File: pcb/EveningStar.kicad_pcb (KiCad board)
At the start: 2 copper layers, 145.5 x 43.6 mm, 152 parts, among them J1 PZ254V-11-02P, J2 Connector, USB-TYPE-C-16P, J3 ESPPROG, J4 RJ45_Hanrun_HR911105A_Horizon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, Q2 AO3400A, U1 TPS5430DDAR, U10 AMS1117-5.0, U11 AMS1117-3.3, U2 SN74HC132DR, U3 ISO6721RBDR, U4 DC-005H-D020, U5 15uH, U6 AHT20-F, U8 ESP32-C6-MINI-1U-H4, U9 W5500, Y1 25MHz

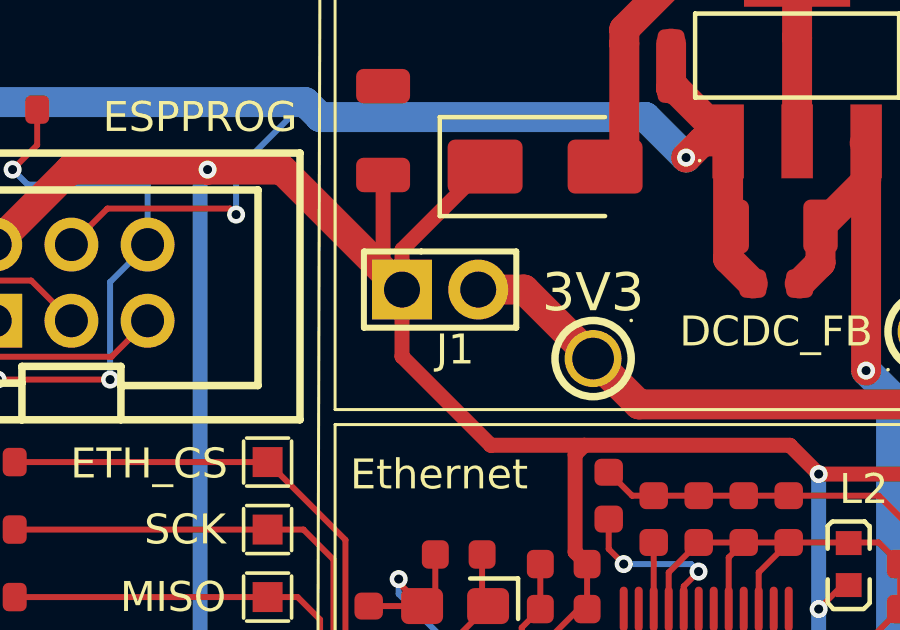
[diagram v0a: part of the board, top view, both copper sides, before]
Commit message: sch: remove 3.3v jumper
Fixes #16
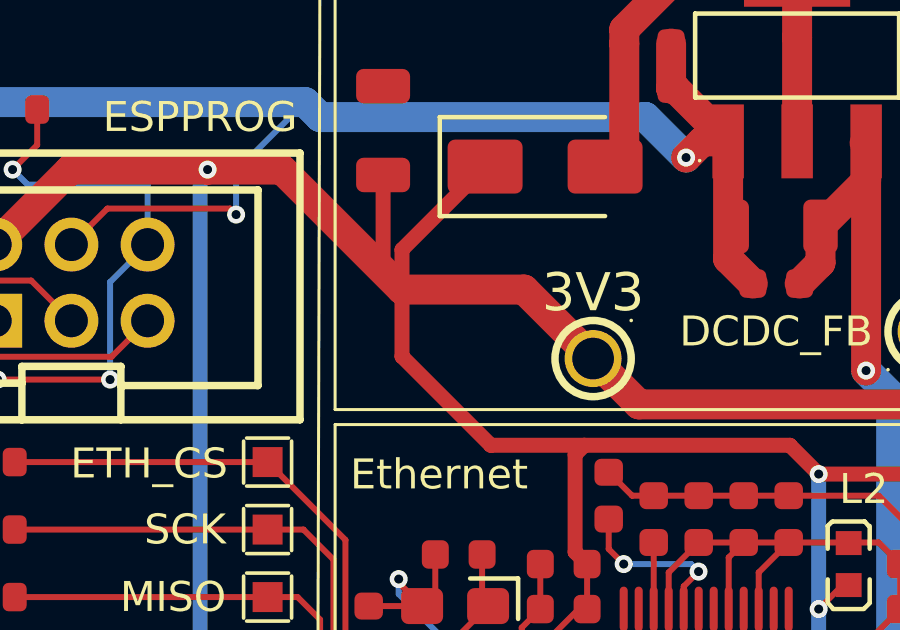
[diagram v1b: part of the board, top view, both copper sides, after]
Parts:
- removed J1: PZ254V-11-02P, EasyEDA:HDR-TH_2P-P2.54-V-M
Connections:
- C36 pad 1: Net-(J1-Pin_2) -> +3V3
- C8 pad 1: Net-(J1-Pin_2) -> +3V3
- R12 pad 1: Net-(J1-Pin_2) -> +3V3
- TP10 pad 1: Net-(J1-Pin_2) -> +3V3
- U5 pad 2: Net-(J1-Pin_2) -> +3V3
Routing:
- net +3V3: track 245.9 -> 282.6 mm
- net Net-(J1-Pin_2): track 34.6 -> 0.00 mm
- added copper zone on F.Cu, net +3V3
- removed copper zone on F.Cu, net Net-(J1-Pin_2)

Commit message: pcb: layout and route meterbus frontend
Places parts PCB traces for MeterBus frontend.
Also changes which gates on HC14 schematic are used to simplify routing.
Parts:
- removed C36, C39: 100uF, PCM_JLCPCB:C_1206
- removed C37: 100nF, PCM_JLCPCB:C_0603
- removed C38: 150pF, PCM_JLCPCB:C_0603
- removed C45: 10uF, PCM_JLCPCB:C_0805
- removed D10, D11: SMAJ28CA, PCM_JLCPCB:D_DO-214AC(SMA)
- removed D14, D8: SS210, PCM_JLCPCB:D_SMA
- removed D9: SS14, PCM_JLCPCB:D_SMA
- removed J3: ESPPROG, EasyEDA:IDC-TH_6P-P2.54-V-R2-C3-S2.54
- removed J4: RJ45_Hanrun_HR911105A_Horizontal, EasyEDA:RJ45-TH_HR911105A
- removed Q2: AO3400A, PCM_JLCPCB:Q_SOT-23
- removed R27: 33Ω, PCM_JLCPCB:R_0603
- removed R28, R29, R30: 10kΩ, PCM_JLCPCB:R_0603
- removed R48: 12kΩ, PCM_JLCPCB:R_0603
- removed R49: 200Ω, PCM_JLCPCB:R_0603
- removed R5: 100Ω, PCM_JLCPCB:R_0603
- removed R53, R54: 2Ω, PCM_JLCPCB:R_0603
- removed S2, S3: Tactile Button, 160gf, PCM_JLCPCB:SW_TS-1088-AR02016
- removed TP1, TP12, TP13, TP2, TP3, TP5, TP6, TP7, TP8, TP9: RH-5001, EasyEDA:TEST-TH_BD2.54-P1.4_BLACK
- removed U10: AMS1117-5.0, EasyEDA:SOT-223_L6.5-W3.5-P2.30-LS7.0-BR
- removed U2: SN74HC132DR, EasyEDA:SOIC-14_L8.7-W3.9-P1.27-LS6.0-BL
- removed U4: DC-005H-D020, EasyEDA:DC-IN-TH_G-SWITCH_DC-005H-D020
- added C11: 20pF, PCM_JLCPCB:C_0603, F.Cu at (809.0, -32.6)
- added C12: 20pF, PCM_JLCPCB:C_0603, F.Cu at (809.0, -30.4)
- added C14: 100nF, PCM_JLCPCB:C_0805, F.Cu at (908.2, -95.6)
- added D1: USBLC6-2P6, EasyEDA:SOT-666-6_L1.6-W1.2-P0.50-LS1.6-BR, F.Cu at (1062.4, -97.3)
- added D15: SS210, PCM_JLCPCB:D_SMA, F.Cu at (926.0, -91.5)
- added D3: SMBJ17CA, EasyEDA:SMB_L4.3-W3.6-LS5.4-BI, F.Cu at (584.5, 24.0)
- added F1: 1A, EasyEDA:FUSE-SMD_L6.1-W2.6, F.Cu at (926.5, -101.1)
- added P1: WJ15EDGRC-3.81-2P, EasyEDA:CONN-TH_2P-P3.81_WJ15EDGRC-3.81-2P, F.Cu at (916.5, -111.6)
- added Q1: 2N7002, PCM_JLCPCB:Q_SOT-23, F.Cu at (605.0, 31.5)
- added R37: 33Ω, PCM_JLCPCB:R_0603, F.Cu at (865.6, 17.9)
- added R50: 33Ω, PCM_JLCPCB:R_0603, F.Cu at (867.9, 17.9)
- added R55: 33Ω, PCM_JLCPCB:R_0603, F.Cu at (812.5, -58.0)
- added R57: 10kΩ, PCM_JLCPCB:R_0603, F.Cu at (812.5, -55.8)
- added R58: 10kΩ, PCM_JLCPCB:R_0603, F.Cu at (812.5, -53.5)
- added R59: 10kΩ, PCM_JLCPCB:R_0603, F.Cu at (812.5, -51.3)
- added R60: 10kΩ, PCM_JLCPCB:R_0603, F.Cu at (970.8, -31.5)
- added R61: 10kΩ, PCM_JLCPCB:R_0603, F.Cu at (970.8, -29.2)
- added R62: 33Ω, PCM_JLCPCB:R_0603, F.Cu at (812.5, -49.0)
- added R63: 33Ω, PCM_JLCPCB:R_0603, F.Cu at (816.2, -58.0)
- added R64: 33Ω, PCM_JLCPCB:R_0603, F.Cu at (816.2, -55.8)
- added R65: 33Ω, PCM_JLCPCB:R_0603, F.Cu at (816.2, -53.5)
- added R66: 10kΩ, PCM_JLCPCB:R_0603, F.Cu at (970.8, -27.0)
- added RJ2: 5201-6P6C, EasyEDA:RJ45-TH_RRCH-5201-6P6C, F.Cu at (593.8, 24.2)
- added TP24: READ_ISO, TestPoint:TestPoint_Pad_D1.0mm, F.Cu at (617.5, 21.0)
- added TP25: GND_ISO, TestPoint:TestPoint_Plated_Hole_D2.0mm, F.Cu at (605.0, 27.5)
- added TP26: MB_PWR_ISO, TestPoint:TestPoint_Plated_Hole_D2.0mm, F.Cu at (584.5, 31.5)
- added TP27: WRITE_ISO, TestPoint:TestPoint_Pad_D1.0mm, F.Cu at (617.5, 23.5)
- added TP28: READ, TestPoint:TestPoint_Pad_D1.0mm, F.Cu at (634.5, 21.0)
- added TP29: WRITE, TestPoint:TestPoint_Pad_D1.0mm, F.Cu at (640.5, 21.2)
- added TP30: MISO, TestPoint:TestPoint_Pad_D1.0mm, F.Cu at (967.5, -34.9)
- added TP31: GND, TestPoint:TestPoint_Plated_Hole_D2.0mm, F.Cu at (975.0, -32.5)
- added TP32: GND, TestPoint:TestPoint_Plated_Hole_D2.0mm, F.Cu at (813.2, -31.4)
- added TP33: FLASH_SCK, TestPoint:TestPoint_Pad_D1.0mm, F.Cu at (967.5, -31.8)
- added TP34: MOSI, TestPoint:TestPoint_Pad_D1.0mm, F.Cu at (815.7, -43.3)
- added TP35: +3V3A, TestPoint:TestPoint_Pad_D1.0mm, F.Cu at (857.7, 15.2)
- added TP36: VIN_PROTECTED, TestPoint:TestPoint_Plated_Hole_D2.0mm, F.Cu at (917.6, -92.9)
- added U7: ESP32-C6-WROOM-1-N8, EasyEDA:WIRELM-SMD_ESP32-C6-WROOM-1, F.Cu at (797.0, -42.8)
- added USB1: GT-USB-7055BB, EasyEDA:USB-C-TH_GT-USB-7055BB, F.Cu at (1062.2, -102.0)
- added X1: 32.768kHz, PCM_JLCPCB:FC-135R_L3.2-W1.5, F.Cu at (793.8, -30.9)
- C10: value 10nF -> 47uF; footprint PCM_JLCPCB:C_0603 -> PCM_JLCPCB:C_1206
- C15: value 10uF -> 47uF; footprint PCM_JLCPCB:C_0603 -> PCM_JLCPCB:C_1206
- C2: value 1uF -> 100nF
- C40: footprint PCM_JLCPCB:C_1206 -> PCM_JLCPCB:C_0603
- C42: value 100nF -> 4.7uF; footprint PCM_JLCPCB:C_0603 -> PCM_JLCPCB:C_1206
- C43: value 10uF -> 4.7uF; footprint PCM_JLCPCB:C_0603 -> PCM_JLCPCB:C_1206
- C8: value 1nF -> 22uF
- C9: value 100nF -> 47uF; footprint PCM_JLCPCB:C_0603 -> PCM_JLCPCB:C_1206
- D2: value PSM712-LF-T7 -> SMBJ40CA_C151262; footprint PCM_JLCPCB:SOT-23-3_L3.0-W1.7-P0.95-LS2.9-BR -> EasyEDA:SMB_L4.6-W3.6-LS5.3-BI
- D7: value SMAJ28CA -> PSM712-LF-T7; footprint PCM_JLCPCB:D_DO-214AC(SMA) -> PCM_JLCPCB:SOT-23-3_L3.0-W1.7-P0.95-LS2.9-BR
- J2: value Connector, USB-TYPE-C-16P -> DEBUG; footprint PCM_JLCPCB:TYPE-C-SMD_HX-TYPE-C-16PIN -> Connector_PinHeader_2.54mm:PinHeader_2x03_P2.54mm_Vertical
- R1: value 100Ω -> 1.8kΩ
- R11: value 100Ω -> 100kΩ
- R12: value 10kΩ -> 0Ω
- R13: value 5.6kΩ -> 10kΩ
- R14: value 300Ω -> 100Ω
- R15: value 10kΩ -> 62kΩ
- R16: value 10kΩ -> 27kΩ
- R2: value 1MΩ -> 100kΩ
- R23: value 33Ω -> 10MΩ
- R24: value 33Ω -> 10kΩ
- R25: value 33Ω -> 0Ω
- R26: value 33Ω -> 62kΩ
- R3: value 100kΩ -> 1MΩ
- R4: value 2MΩ -> 2.4kΩ
- R51: value 470Ω -> 33Ω
- R52: value 75Ω -> 10kΩ
- R6: value 330Ω -> 10kΩ
- R7: value 100kΩ -> 0Ω
- R8: value 330Ω -> 33Ω
- RJ1: value 5301-6P6C -> GR01M1HXA001; footprint EasyEDA:RJ45-TH_5301-6P6C -> EasyEDA:RJ45-TH_GR01M1HXA001
- TP10: value RH-5001 -> ETH_CS; footprint EasyEDA:TEST-TH_BD2.54-P1.4_BLACK -> TestPoint:TestPoint_Pad_D1.0mm
- TP11: value RH-5001 -> ETH_RST; footprint EasyEDA:TEST-TH_BD2.54-P1.4_BLACK -> TestPoint:TestPoint_Pad_D1.0mm
- TP14: value RH-5001 -> ETH_SCK; footprint EasyEDA:TEST-TH_BD2.54-P1.4_BLACK -> TestPoint:TestPoint_Pad_D1.0mm
- TP15: value RH-5001 -> FLASH_CS; footprint EasyEDA:TEST-TH_BD2.54-P1.4_BLACK -> TestPoint:TestPoint_Pad_D1.0mm
- TP16: value RH-5001 -> MISO; footprint EasyEDA:TEST-TH_BD2.54-P1.4_BLACK -> TestPoint:TestPoint_Pad_D1.0mm
- TP17: value RH-5001 -> MOSI; footprint EasyEDA:TEST-TH_BD2.54-P1.4_BLACK -> TestPoint:TestPoint_Pad_D1.0mm
- TP18: value TestPad -> ETH_INT; footprint EasyEDA:TestPoint_Pad_1.0x1.0mm -> TestPoint:TestPoint_Pad_D1.0mm
- TP19: value TestPad -> GND; footprint EasyEDA:TestPoint_Pad_1.0x1.0mm -> TestPoint:TestPoint_Plated_Hole_D2.0mm
- TP20: value TestPad -> MISO; footprint EasyEDA:TestPoint_Pad_1.0x1.0mm -> TestPoint:TestPoint_Pad_D1.0mm
- TP21: value TestPad -> VCC_ISO; footprint EasyEDA:TestPoint_Pad_1.0x1.0mm -> TestPoint:TestPoint_Pad_D1.0mm
- TP22: value TestPad -> BUS_ISO; footprint EasyEDA:TestPoint_Pad_1.0x1.0mm -> TestPoint:TestPoint_Pad_D1.0mm
- TP23: value TestPad -> MOSI; footprint EasyEDA:TestPoint_Pad_1.0x1.0mm -> TestPoint:TestPoint_Pad_D1.0mm
- U1: value TPS5430DDAR -> 78L05G; footprint EasyEDA:ESOP-8_L4.9-W3.9-P1.27-LS6.0-TL-EP -> PCM_JLCPCB:SOT-89-3_L4.5-W2.5-P1.50-LS4.2-BR
- U11: value AMS1117-3.3 -> 15uH; footprint EasyEDA:SOT-223_L6.5-W3.5-P2.30-LS7.0-BR -> EasyEDA:IND-SMD_L7.1-W6.6
- U5: value 15uH -> 74HC14D; footprint EasyEDA:IND-SMD_L7.1-W6.6 -> PCM_JLCPCB:SOIC-14_L8.7-W3.9-P1.27-LS6.0-BL
- U6: value AHT20-F -> LMR38020SDDAR; footprint EasyEDA:SENSOR-SMD-6_AHT20 -> EasyEDA:ESOP-8_L4.9-W3.9-P1.27-LS6.0-BL-EP-1
- U8: value ESP32-C6-MINI-1U-H4 -> GD5F2GM7UEYIGR; footprint EasyEDA:WIFIM-SMD_61P-L13.2-W12.5-P0.80 -> EasyEDA:WSON-8_L8.0-W6.0-P1.27-TL-1
- U9: footprint EasyEDA:LQFP-48_L7.0-W7.0-P0.50-LS9.0-BL -> Package_QFP:LQFP-48_7x7mm_P0.5mm
- moved R18 973.2 mm to (1059.0, -97.6), turned to 0 degrees
- moved R19 967.2 mm to (1059.0, -95.4), turned to 0 degrees
- moved TP15 899.8 mm to (967.5, -41.0)
- moved U8 877.5 mm to (975.1, -38.7)
- moved H4 852.5 mm to (872.8, 238.8)
- moved TP23 850.1 mm to (967.5, -37.9)
- moved C40 842.7 mm to (979.2, -33.8), turned to 0 degrees
- moved C41 842.6 mm to (979.2, -31.5), turned to 0 degrees
- moved D2 839.3 mm to (925.8, -96.2), turned to 0 degrees
- moved R11 835.4 mm to (913.5, -102.3), turned to 0 degrees
- moved G*** 834.0 mm to (965.5, 115.2)
- moved C15 829.0 mm to (908.8, -105.5)
- moved R15 820.4 mm to (913.5, -100.1), turned to 0 degrees
- moved R16 820.3 mm to (913.5, -97.8), turned to 0 degrees
- moved R51 817.6 mm to (970.8, -33.8)
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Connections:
- net /ethernet/RXN1 renamed Net-(C32-Pad1)
- net /ethernet/RXP1 renamed Net-(C31-Pad1)
- net Net-(U9-1V2O) renamed /ethernet/1V2REG
- net Net-(U9-TOCAP) renamed /ethernet/TOCAP
- net Net-(U9-XI/CLKIN) renamed /ethernet/XI
- net Net-(U9-XO) renamed /ethernet/XO
- C1 pad 1: +PROT_BATT_ISO -> Net-(U1-VIN)
- C10 pad 1: Net-(U1-BOOT) -> Net-(C10-Pad1)
- C10 pad 2: Net-(U1-PH) -> GND
- C13 pad 1: +3V3 -> Net-(U6-SW)
- C13 pad 2: GND -> Net-(U6-BOOT)
- C15 pad 1: GND -> Net-(C10-Pad1)
- C15 pad 2: +3V3 -> GND
- C2 pad 1: /mcu/MCU_RESET -> /mcu/MCU_RST
- C29 pad 1: Net-(J4-RCT) -> /ethernet/RCT
- C3 pad 1: +5V_ISO -> VCC_ISO
- C34 pad 1: Net-(J4-TCT) -> /ethernet/TCT
- C35 pad 1: +PROT_BATT_ISO -> Net-(U1-VIN)
- C4 pad 1: +5V_ISO -> VCC_ISO
- C40 pad 1: USB_PWR -> GND
- C40 pad 2: GND -> +3V3
- C41 pad 1: USB_PWR -> +3V3
- C42 pad 1: Net-(U11-VOUT) -> Net-(U6-EN)
- C43 pad 1: Net-(U11-VOUT) -> Net-(U6-EN)
- C5 pad 1: +5V_ISO -> VCC_ISO
- C7 pad 1: +5V_ISO -> VCC_ISO
- C8 pad 1: +3V3 -> GND
- C8 pad 2: Net-(U1-VSENSE) -> +3V3
- C9 pad 1: Net-(U1-VIN) -> Net-(C10-Pad1)
- D2 pad 1: /mcu/USB_D- -> GND
- D2 pad 2: /mcu/USB_D+ -> Net-(D2-A)
- D5 pad 1: +PROT_BATT_ISO -> Net-(U1-VIN)
- D5 pad 2: +BATT_ISO -> MB_PWR_ISO
- D7 pad 1: GND -> /meterbus_frontend/BUS_ISO
- D7 pad 2: Net-(D14-Pad2) -> /meterbus_frontend/BUS_ISO
- R1 pad 1: Net-(Q2-D) -> Net-(R1-Pad1)
- R1 pad 2: Net-(D10-Pad2) -> Net-(D4-Pad2)
- R10 pad 2: MB_WRITE -> /mcu/WRITE
- R11 pad 1: /mcu/MCU_RESET -> Net-(C10-Pad1)
- R11 pad 2: Net-(S2-A) -> /mcu/PGOOD
- R12 pad 1: +3V3 -> /mcu/PGOOD
- R12 pad 2: Net-(U1-VSENSE) -> /mcu/MCU_RST
- R13 pad 1: Net-(R13-Pad1) -> Net-(D6-Pad2)
- R13 pad 2: GND -> /meterbus_frontend/READ_ISO
- R14 pad 1: Net-(U1-VSENSE) -> Net-(Q1-G)
- R14 pad 2: Net-(R13-Pad1) -> Net-(R1-Pad1)
- R15 pad 1: +3V3 -> Net-(C10-Pad1)
- R15 pad 2: /mcu/SDA -> Net-(U6-FB)
- R16 pad 1: +3V3 -> Net-(U6-FB)
- R16 pad 2: /mcu/SCL -> GND
- R17 pad 1: +3V3 -> /mcu/MCU_RST
- R17 pad 2: /mcu/MCU_RESET -> +3V3
- R18 pad 1: Net-(J2-CC1) -> Net-(USB1-CC1)
- R19 pad 1: Net-(J2-CC2) -> Net-(USB1-CC2)
- R2 pad 1: Net-(D10-Pad2) -> Net-(Q1-G)
- R2 pad 2: Net-(R2-Pad2) -> GND_ISO
- R20 pad 2: /mcu/IO9 -> /mcu/BOOT9
- R21 pad 2: /mcu/IO8 -> /mcu/BOOT8
- R22 pad 2: Net-(U8-IO0) -> /mcu/LED
- R23 pad 1: Net-(U8-IO18) -> /mcu/XTAL_32K_N
- R23 pad 2: MOSI -> /mcu/XTAL_32K_P
- R24 pad 1: Net-(U8-IO19) -> +3V3
- R24 pad 2: SCK -> /mcu/JTAG_SRC
- R25 pad 1: Net-(U8-IO20) -> Net-(C10-Pad1)
- R25 pad 2: MISO -> +3V3
- R26 pad 1: Net-(U8-IO21) -> Net-(U6-RT/SYNC)
- R26 pad 2: ETH_CS -> GND
- R3 pad 1: Net-(Q2-G) -> /meterbus_frontend/BUS_ISO
- R38 pad 2: Net-(J4-RCT) -> /ethernet/RCT
- R4 pad 1: Net-(R2-Pad2) -> /ethernet/EXRES1
- R4 pad 2: GND_ISO -> Net-(R4-Pad2)
- R43 pad 2: Net-(J4-RCT) -> /ethernet/RCT
- R45 pad 2: Net-(J4-TCT) -> /ethernet/TCT
- R46 pad 1: Net-(J4-Pad11) -> Net-(R46-Pad1)
- R47 pad 1: Net-(J4-Pad10) -> Net-(R47-Pad1)
- R51 pad 1: Net-(C37-Pad2) -> /flash/MISO
- R51 pad 2: Net-(R51-Pad2) -> Net-(U8-SO/SIO1)
- R52 pad 1: Net-(R51-Pad2) -> GND
- R52 pad 2: Net-(R52-Pad2) -> Net-(R4-Pad2)
- R6 pad 1: Net-(R5-Pad2) -> /meterbus_frontend/BUS_ISO
- R6 pad 2: Net-(D4-Pad2) -> Net-(R6-Pad2)
- R7 pad 1: +5V_ISO -> Net-(J2-Pin_2)
- R7 pad 2: Net-(U3-INA) -> +3V3
- R8 pad 1: Net-(U3-INA) -> /meterbus_frontend/BUS_ISO
- R8 pad 2: Net-(D6-Pad2) -> Net-(Q1-D)
- R9 pad 2: MB_READ -> /mcu/READ
- RJ1 pad 1: GND_ISO -> /ethernet/TD+
- RJ1 pad 2: GND_ISO -> /ethernet/TD-
- RJ1 pad 3: Net-(D10-Pad2) -> /ethernet/TCT
- RJ1 pad 4: GND_ISO -> unconnected-(RJ1-NC-Pad4)
- RJ1 pad 5: +BATT_ISO -> /ethernet/RCT
- RJ1 pad 6: +BATT_ISO -> /ethernet/RD+
- S1 pad 1: Net-(S1-A) -> /mcu/CFG
- TP10 pad 1: +3V3 -> /ethernet/CS
- TP11 pad 1: /mcu/MCU_RESET -> /mcu/ETH_RST
- TP14 pad 1: Net-(U3-INA) -> /ethernet/SCK
- TP15 pad 1: Net-(U3-OUTB) -> /flash/CS
- TP16 pad 1: MB_WRITE -> /mcu/MCU_MISO
- TP17 pad 1: MB_READ -> /ethernet/MOSI
- TP18 pad 1: MOSI -> /ethernet/INT
- TP19 pad 1: SCK -> GND
- TP20 pad 1: MISO -> /ethernet/MISO
- TP21 pad 1: ETH_CS -> VCC_ISO
- TP22 pad 1: ETH_INT -> /meterbus_frontend/BUS_ISO
- TP23 pad 1: ETH_RST -> /flash/MOSI
- U1 pad 1: Net-(U1-BOOT) -> VCC_ISO
- U11 pad 1: GND -> Net-(U6-SW)
- U11 pad 2: Net-(U11-VOUT) -> Net-(C10-Pad1)
- U3 pad 1: +5V_ISO -> VCC_ISO
- U3 pad 2: Net-(U3-INA) -> /meterbus_frontend/READ_ISO
- U3 pad 3: Net-(U3-OUTB) -> /meterbus_frontend/WRITE_ISO
- U3 pad 6: MB_WRITE -> /mcu/WRITE
- U3 pad 7: MB_READ -> /mcu/READ
- U5 pad 1: Net-(U1-PH) -> GND_ISO
- U5 pad 2: +3V3 -> unconnected-(U5-Pad2)
- U6 pad 1: unconnected-(U6-NC-Pad1) -> GND
- U6 pad 2: +3V3 -> Net-(U6-EN)
- U6 pad 3: /mcu/SCL -> Net-(U6-EN)
- U6 pad 4: /mcu/SDA -> Net-(U6-RT/SYNC)
- U6 pad 5: GND -> Net-(U6-FB)
- U6 pad 6: unconnected-(U6-NC-Pad6) -> /mcu/PGOOD
- U8 pad 1: GND -> /flash/CS
- U8 pad 2: GND -> Net-(U8-SO/SIO1)
- U8 pad 3: +3V3 -> Net-(U8-~{WP}/SIO2)
- U8 pad 4: unconnected-(U8-NC-Pad4) -> GND
- U8 pad 5: /mcu/SDA -> /flash/MOSI
- U8 pad 6: /mcu/SCL -> /flash/SCK
- U8 pad 7: unconnected-(U8-NC-Pad7) -> Net-(U8-~{HOLD}/SIO3)
- U8 pad 8: /mcu/MCU_RESET -> +3V3
- U9 pad 10: Net-(U9-EXRES1) -> /ethernet/EXRES1
- U9 pad 23: unconnected-(U9-RSVD-Pad23) -> GND
- U9 pad 32: ETH_CS -> /ethernet/CS
- U9 pad 33: SCK -> /ethernet/SCK
- U9 pad 34: MISO -> Net-(U9-MISO)
- U9 pad 35: MOSI -> /ethernet/MOSI
- U9 pad 36: ETH_INT -> Net-(U9-~{INT})
- U9 pad 37: ETH_RST -> /mcu/ETH_RST
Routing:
- net GND: track 353.9 -> 108.1 mm, vias 26 -> 14
- net +3V3: track 282.6 -> 101.3 mm, vias 10 -> 3
- net USB_PWR: track 85.8 -> 0.00 mm, vias 4 -> 0
- net /mcu/SDA: track 59.6 -> 0.00 mm, vias 5 -> 0
- net /mcu/SCL: track 57.8 -> 0.00 mm, vias 7 -> 0
- net Net-(R1-Pad1): track 0.00 -> 52.0 mm, vias 0 -> 2
- net /mcu/IO9: track 48.6 -> 0.00 mm, vias 8 -> 0
- net ETH_RST: track 46.4 -> 0.00 mm, vias 2 -> 0
- net (no net): track 0.00 -> 43.3 mm, vias 0 -> 1
- net /mcu/MCU_RESET: track 42.1 -> 0.00 mm, vias 4 -> 0
- net +5V_ISO: track 40.6 -> 0.00 mm
- net Net-(J4-Pad11): track 39.2 -> 0.00 mm
- net Net-(R46-Pad1): track 0.00 -> 39.2 mm
- net MB_WRITE: track 38.9 -> 0.00 mm, vias 4 -> 0
- net GND_ISO: track 101.7 -> 140.2 mm
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- removed copper zone on F.Cu, net +3V3
- removed copper zone on B.Cu, net GND
- removed copper zone on F.Cu, net Net-(U1-PH)
- removed copper zone on F.Cu, net Net-(U1-VIN)
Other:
- board size 145.5 x 43.6 mm -> 306.5 x 249 mm
- board text removed: "Ethernet"
- board text removed: "MeterBus Frontend"
- board text removed: "Power Supply"
- board text removed: "Processor"

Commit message: pcb: fix 3d models
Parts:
- moved USB1 369.3 mm to (742.5, 82.8), turned to 180 degrees
- moved D1 364.9 mm to (742.3, 78.0), turned to 180 degrees
- moved C10 360.6 mm to (587.5, 54.8)
- moved C13 360.6 mm to (586.5, 70.7)
- moved C14 360.6 mm to (586.9, 68.1)
- moved C15 360.6 mm to (587.5, 58.2)
- moved C42 360.6 mm to (587.5, 61.5)
- moved C43 360.6 mm to (587.5, 64.9)
- moved C9 360.6 mm to (587.5, 51.5)
- moved D15 360.6 mm to (604.6, 72.1)
- moved D2 360.6 mm to (604.5, 67.4)
- moved F1 360.6 mm to (605.2, 62.6)
- moved P1 360.6 mm to (595.1, 52.0)
- moved R11 360.6 mm to (592.1, 61.3)
- moved R15 360.6 mm to (592.1, 63.6)
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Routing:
- net GND: vias 14 -> 9
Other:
- board size 306.5 x 249 mm -> 107 x 97.2 mm

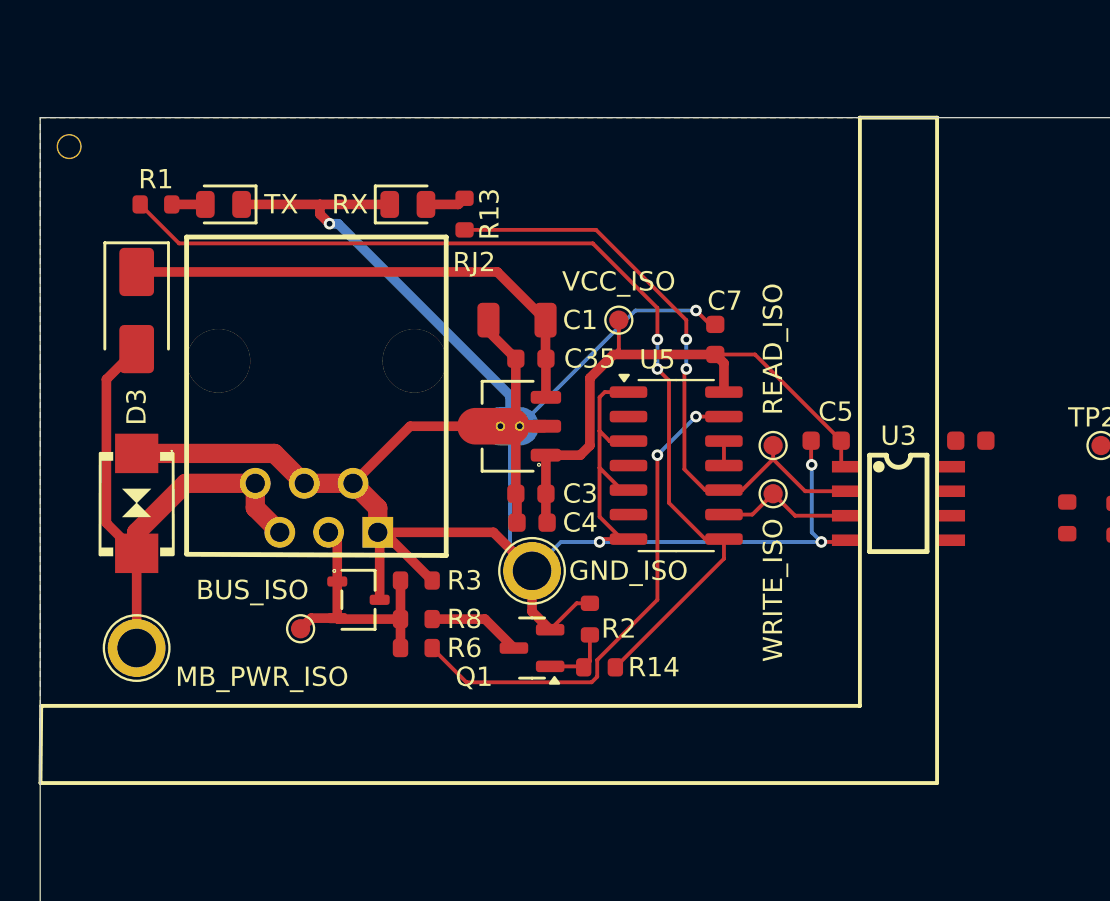
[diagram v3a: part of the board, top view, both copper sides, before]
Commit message: pcb: compact meterbus frontend layout
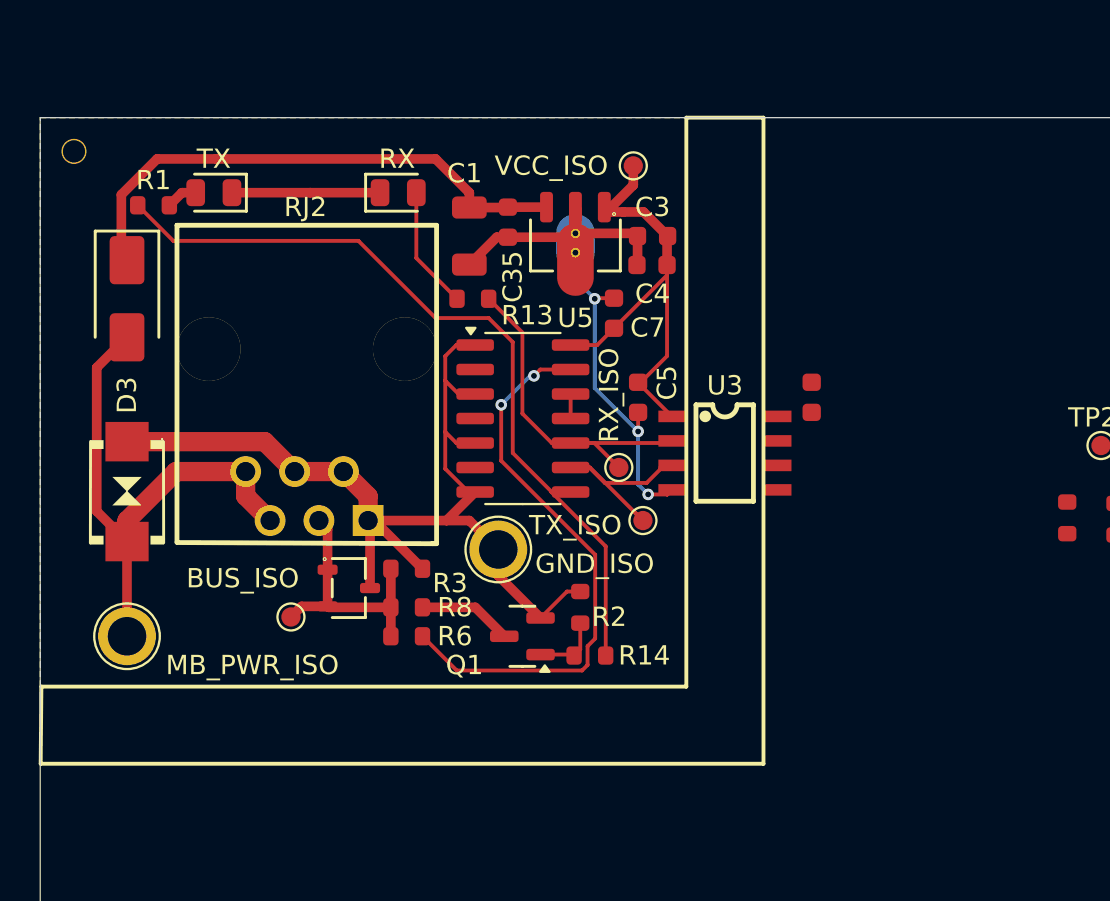
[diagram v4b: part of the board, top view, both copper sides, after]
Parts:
- TP24: value READ_ISO -> RX_ISO
- TP27: value WRITE_ISO -> TX_ISO
- moved C3 14.8 mm to (611.2, 10.1)
- moved C4 14.7 mm to (611.2, 11.6)
- moved U1 10.4 mm to (607.2, 10.0), turned to 90 degrees
- moved C5 10.0 mm to (610.5, 18.5), turned to -90 degrees
- moved U3 9.37 mm to (615.0, 21.4)
- moved C6 8.55 mm to (619.5, 18.5), turned to 90 degrees
- moved U5 8.32 mm to (604.5, 19.6)
- moved TP24 8.08 mm to (609.5, 22.1)
- moved TP21 8.04 mm to (610.2, 6.50)
- moved C35 7.18 mm to (603.8, 9.42), turned to -90 degrees
- moved TP27 6.89 mm to (610.8, 24.9)
- moved C7 5.42 mm to (609.2, 14.1)
- moved C1 5.01 mm to (601.8, 10.1), turned to -90 degrees
- moved R13 4.41 mm to (601.9, 13.4), turned to 0 degrees
- moved TP25 2.07 mm to (603.2, 26.4)
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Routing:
- net GND_ISO: track 140.2 -> 90.1 mm, vias 5 -> 3
- net /meterbus_frontend/READ_ISO: track 32.1 -> 18.3 mm, vias 2 -> 0
- net Net-(R1-Pad1): track 52.0 -> 42.9 mm, vias 2 -> 0
- net VCC_ISO: track 30.4 -> 24.7 mm
- net /meterbus_frontend/WRITE_ISO: track 7.22 -> 11.7 mm
- net Net-(D6-Pad2): track 2.13 -> 6.37 mm
- net Net-(R6-Pad2): track 26.5 -> 29.4 mm
- net Net-(U1-VIN): track 26.2 -> 27.8 mm

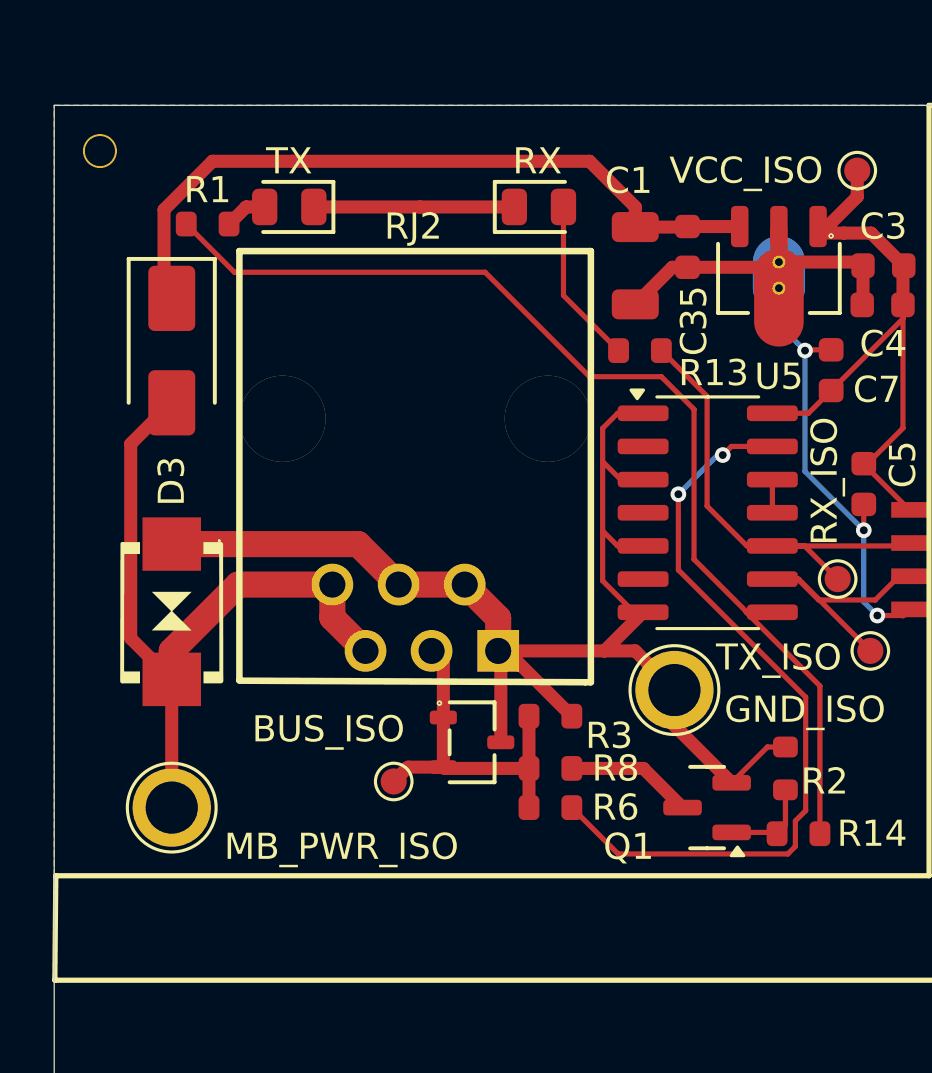
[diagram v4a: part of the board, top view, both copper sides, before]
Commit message: pcb: adjust drc rules to match jlc
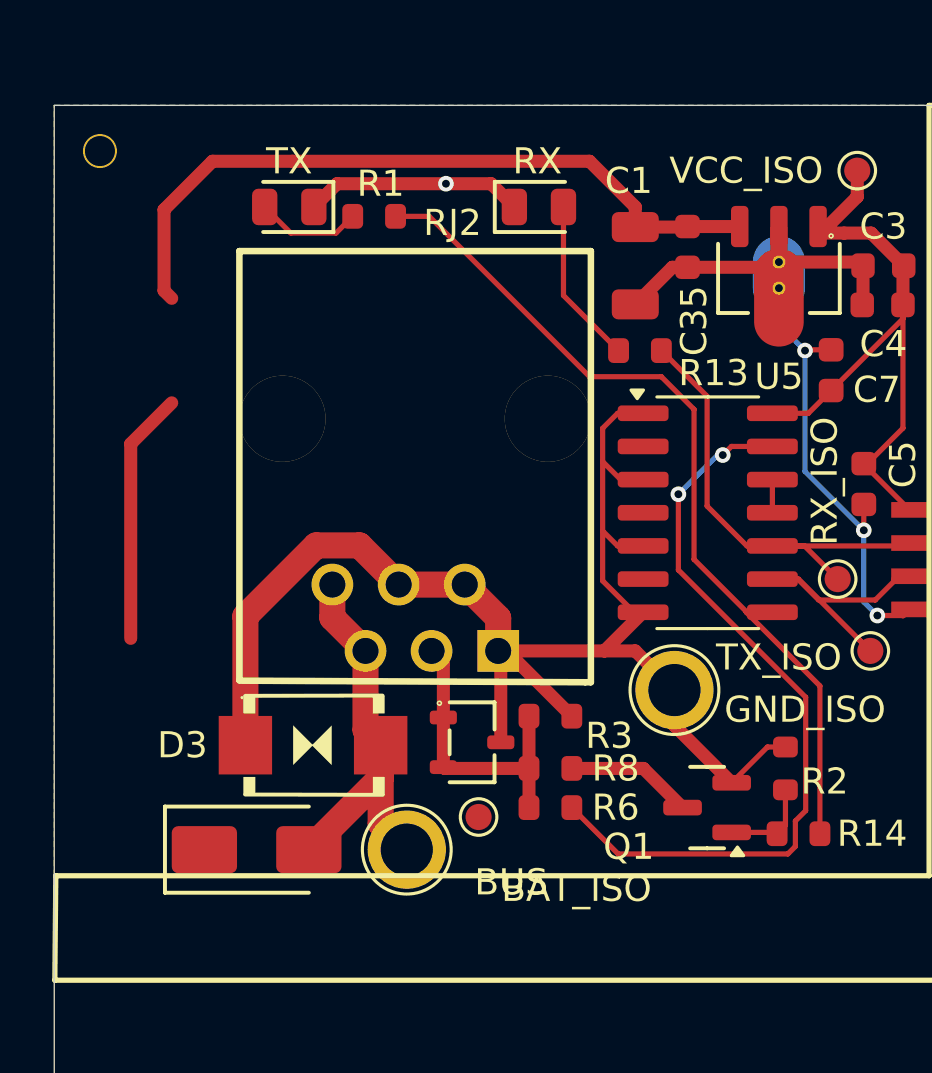
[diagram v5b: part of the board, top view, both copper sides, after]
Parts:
- TP22: value BUS_ISO -> BUS
- TP26: value MB_PWR_ISO -> BAT_ISO
- moved D5 19.4 mm to (587.2, 32.5), turned to 0 degrees
- moved TP26 9.14 mm to (593.0, 32.5)
- moved D3 7.44 mm to (589.4, 28.5), turned to 0 degrees
- moved R1 6.38 mm to (591.8, 8.25), turned to 180 degrees
- moved TP22 3.52 mm to (595.8, 31.2)
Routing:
- net Net-(R1-Pad1): track 42.9 -> 34.7 mm
- net GND_ISO: track 90.1 -> 94.0 mm, vias 3 -> 4
- net Net-(D4-Pad2): track 1.64 -> 4.05 mm
- net /meterbus_frontend/BUS_ISO: track 13.6 -> 11.4 mm
- net MB_PWR_ISO: track 28.2 -> 26.1 mm

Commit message: pcb(mb_frontend): optimise layout
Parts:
- TP26: value BAT_ISO -> BAT
- moved C4 544.2 mm to (68.6, 53.1)
- moved RJ2 544.2 mm to (50.7, 65.1)
- moved C1 544.2 mm to (59.1, 51.6)
- moved C3 544.2 mm to (68.6, 51.6)
- moved C35 544.2 mm to (61.1, 50.9)
- moved C5 544.2 mm to (67.8, 60.0)
- moved C6 544.2 mm to (76.8, 60.0)
- moved C7 544.2 mm to (66.6, 55.6)
- moved D3 544.2 mm to (46.8, 70.0)
- moved D4 544.2 mm to (45.9, 49.4)
- moved D5 544.2 mm to (44.6, 74.0)
- moved D6 544.2 mm to (55.4, 49.4)
- moved D7 544.2 mm to (52.9, 69.9)
- moved Q1 544.2 mm to (61.9, 72.4)
- moved R1 544.2 mm to (49.1, 49.8)
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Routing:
- net Net-(U1-VIN): track 27.8 -> 47.0 mm
- net MB_PWR_ISO: track 26.1 -> 16.5 mm
- net /meterbus_frontend/BUS_ISO: track 11.4 -> 13.8 mm
- net VCC_ISO: track 24.7 -> 23.1 mm

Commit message: pcb(mb_frontend): optimise layout
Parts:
- moved R8 3.04 mm to (58.4, 72.5)
- moved R6 2.88 mm to (58.4, 71.1)
- moved TP21 2.15 mm to (66.5, 49.3)
- moved C1 2.15 mm to (57.0, 51.5)
- moved C35 2.15 mm to (59.0, 50.8)
- moved D3 2.15 mm to (44.6, 69.9)
- moved D4 2.15 mm to (43.7, 49.3)
- moved D6 2.15 mm to (53.3, 49.3)
- moved D7 2.15 mm to (50.7, 69.8)
- moved R1 2.15 mm to (47.0, 49.7)
- moved R13 2.15 mm to (57.1, 54.8)
- moved R3 2.15 mm to (53.7, 68.8)
- moved RJ2 2.15 mm to (48.5, 65.0)
- moved TP25 2.15 mm to (58.5, 67.8)
- moved U5 2.15 mm to (59.7, 61.0)
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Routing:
- net Net-(R6-Pad2): track 29.4 -> 16.6 mm
- net /meterbus_frontend/BUS_ISO: track 13.8 -> 19.0 mm
- net Net-(Q1-D): track 4.86 -> 0.00 mm
- net GND_ISO: track 94.0 -> 96.2 mm, vias 4 -> 5
- net MB_PWR_ISO: track 16.5 -> 14.6 mm
- net Net-(U1-VIN): track 47.0 -> 48.4 mm
- net Net-(Q1-G): track 3.57 -> 4.57 mm
- net Net-(R1-Pad1): track 34.7 -> 35.7 mm
